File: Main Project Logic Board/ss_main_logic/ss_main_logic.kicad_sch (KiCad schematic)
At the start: 17 parts, among them J1 Conn_01x06_Pin, J2 KeyPAD, J3 Conn_01x03_Pin, J4 Conn_01x03_Pin, J5 Screw_Terminal_01x02, J6 Conn_01x03_Pin, U1 PIC24FJ128GA010-I_PT, U2 RN4870-V_RM118

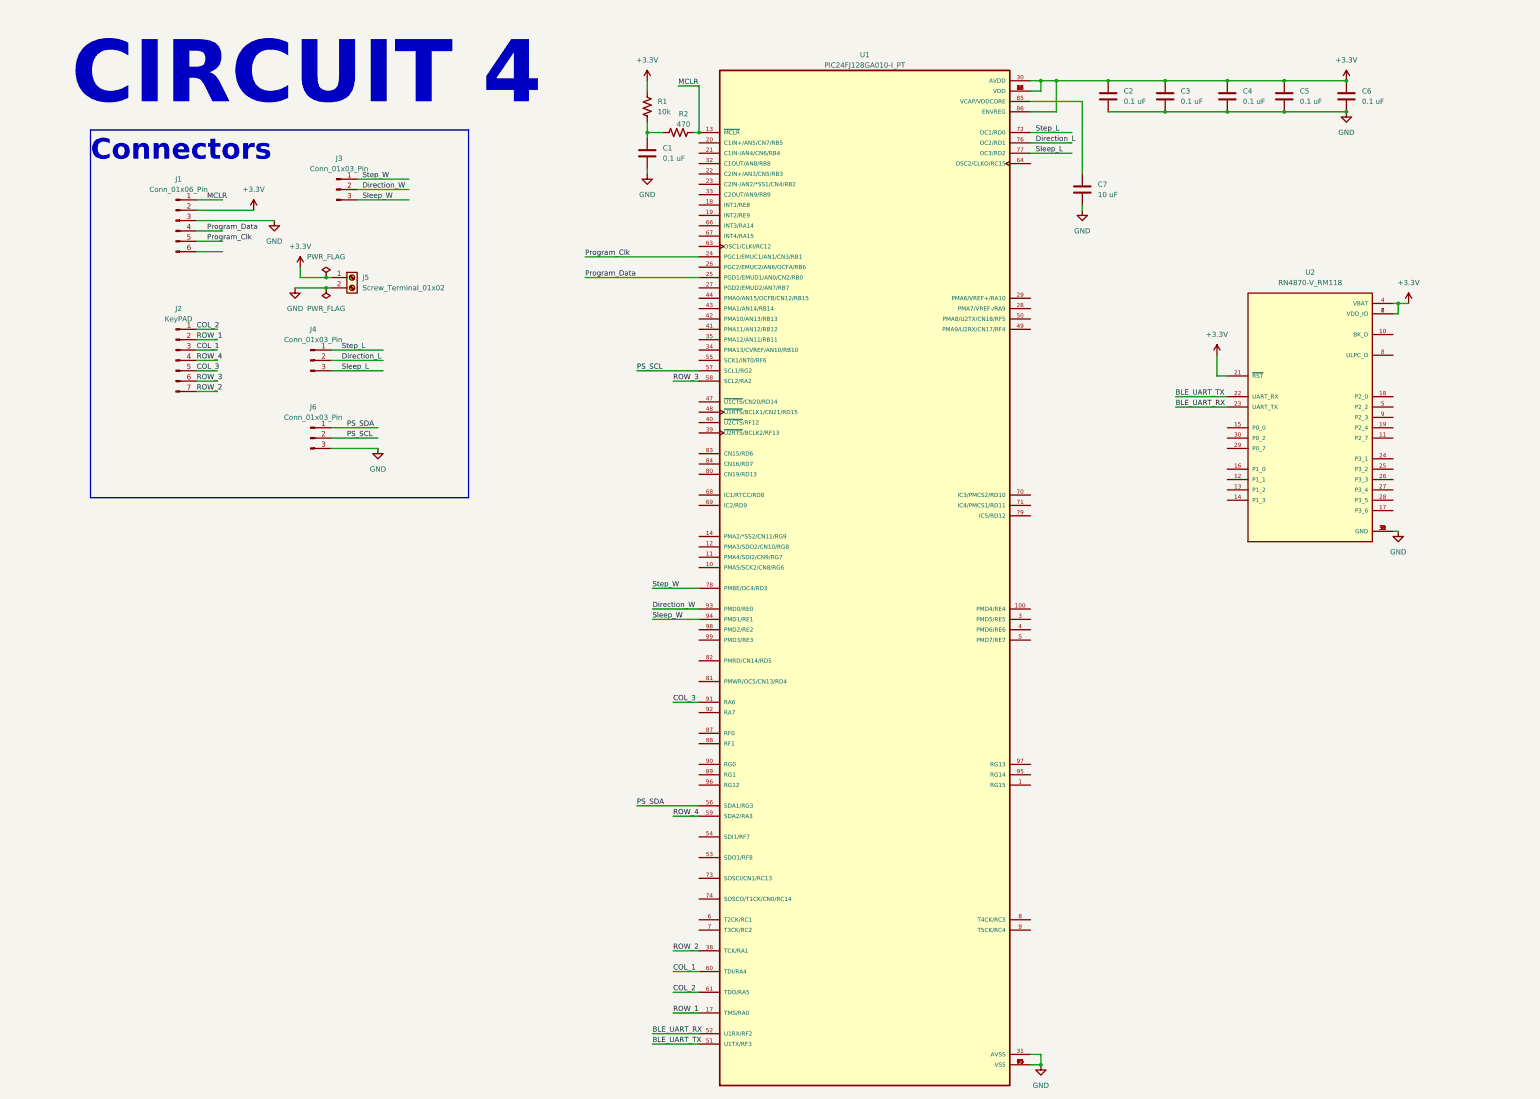
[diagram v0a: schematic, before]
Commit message: Added different BLE and LEDs
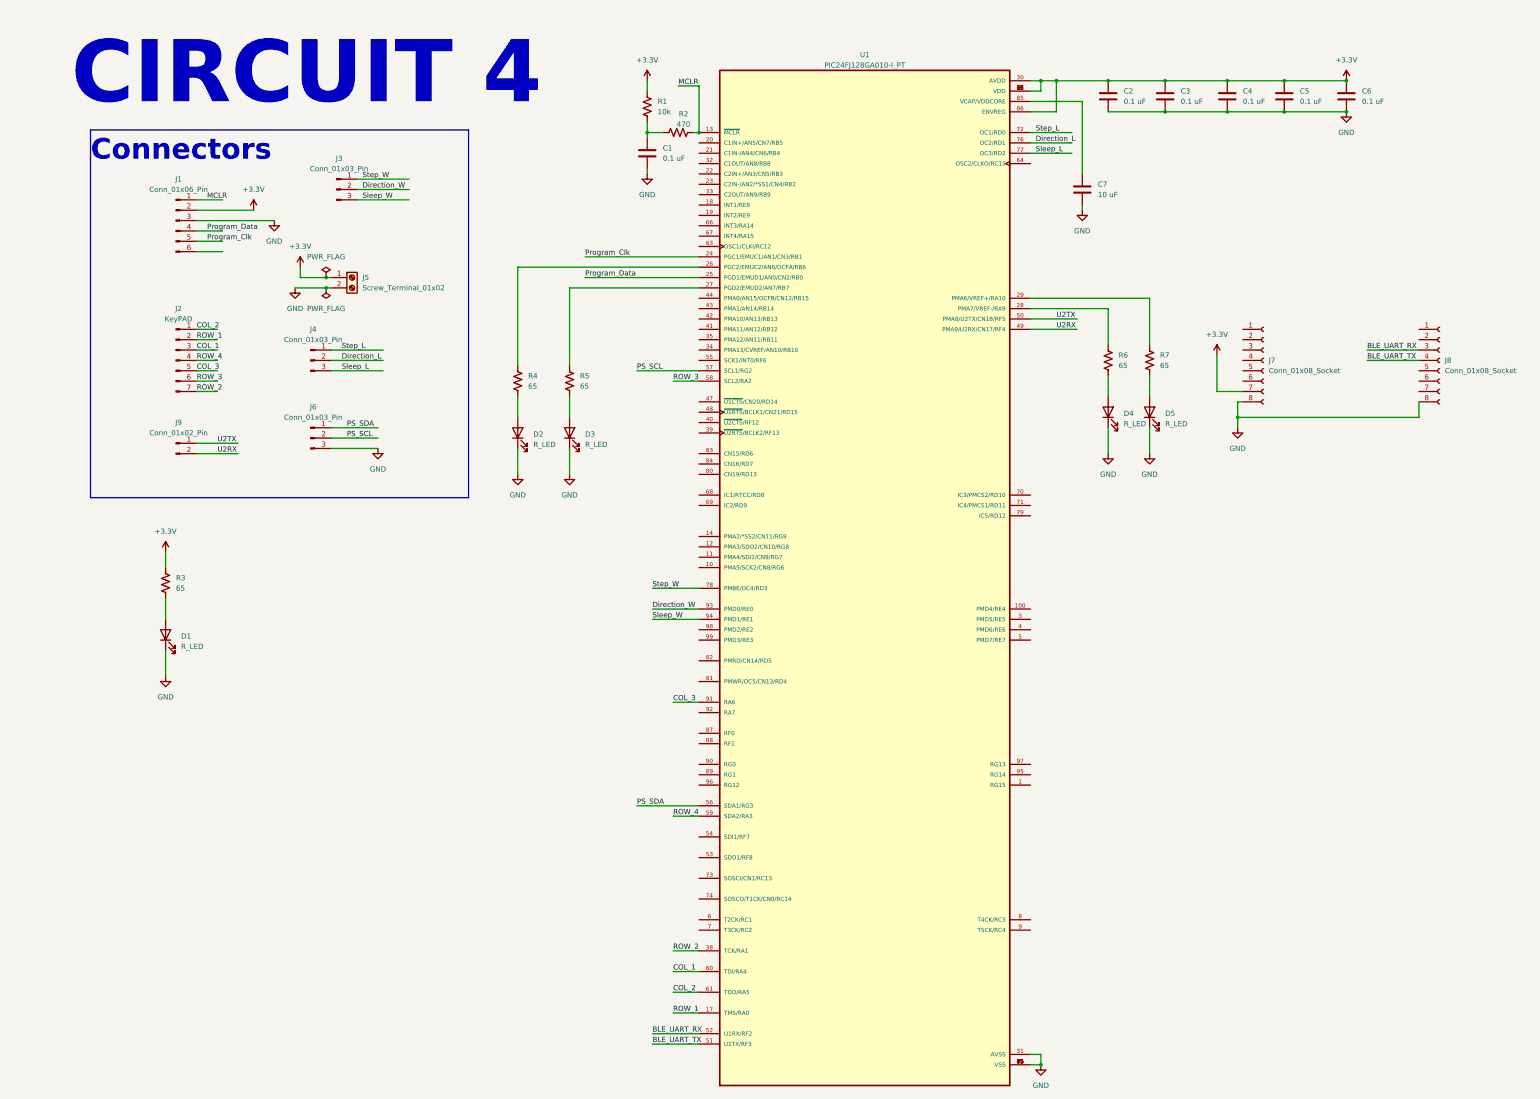
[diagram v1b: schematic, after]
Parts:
- removed U2: RN4870-V_RM118, footprints:RN4870_MCH, symbol RN4870-V_RM118:RN4870-V_RM118
- added D1, D2, D3, D4, D5: R_LED, LED_SMD:LED_0603_1608Metric, symbol Device:LED
- added J7, J8: Conn_01x08_Socket, Connector_PinSocket_2.54mm:PinSocket_1x08_P2.54mm_Vertical, symbol Connector:Conn_01x08_Socket
- added J9: Conn_01x02_Pin, Connector_PinHeader_2.54mm:PinHeader_1x02_P2.54mm_Vertical, symbol Connector:Conn_01x02_Pin
- added R3, R4, R5, R6, R7: 65, Resistor_SMD:R_1210_3225Metric, symbol Device:R_US
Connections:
- net +3.3V: now also J7.7 (Pin_7), R3.1
- net BLE_UART_RX: now also J8.3 (Pin_3)
- net BLE_UART_TX: now also J8.4 (Pin_4)
- net GND: now also D1.1 (K), D2.1 (K), D3.1 (K), D4.1 (K), D5.1 (K), J7.8 (Pin_8), J8.8 (Pin_8)
- net at U1.26 (PGC2/EMUC2/AN6/OCFA/RB6): now also R4.1
- net at U1.27 (PGD2/EMUD2/AN7/RB7): now also R5.1
- net at U1.28 (PMA7/VREF-/RA9): now also R6.1
- net at U1.29 (PMA6/VREF+/RA10): now also R7.1
- net U2RX: now reaches U1.49 (PMA9/U2RX/CN17/RF4)
- net U2RX: now also J9.2 (Pin_2)
- net U2TX: now reaches U1.50 (PMA8/U2TX/CN18/RF5)
- net U2TX: now also J9.1 (Pin_1)
- new net: D2.2 (A), R4.2
- new net: D1.2 (A), R3.2
- new net: D4.2 (A), R6.2
- new net: D3.2 (A), R5.2
- new net: D5.2 (A), R7.2
